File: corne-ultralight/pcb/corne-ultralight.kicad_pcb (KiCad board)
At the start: 2 copper layers, 275.5 x 105.6 mm, 130 parts, among them J2 OLED, J5 Breakaway_Tabs, J7 OLED, SW1 SW_PUSH, SW10 SW_PUSH, SW11 SW_PUSH, SW12 SW_PUSH, SW13 SW_PUSH, SW14 SW_PUSH, SW15 SW_PUSH, SW16 SW_PUSH, SW17 SW_PUSH, SW18 SW_PUSH, SW19 SW_PUSH, SW2 SW_PUSH, SW20 SW_PUSH, SW21 SW_PUSH, SW22 SW_PUSH, SW23 SW_PUSH, SW24 SW_PUSH, SW25 SW_PUSH, SW26 SW_PUSH, SW27 SW_PUSH, SW28 SW_PUSH, SW29 SW_PUSH, SW3 SW_PUSH, SW30 SW_PUSH, SW31 SW_PUSH, SW32 SW_PUSH, SW33 SW_PUSH, SW34 SW_PUSH, SW35 SW_PUSH, SW36 SW_PUSH, SW37 SW_PUSH, SW38 SW_PUSH, SW39 SW_PUSH, SW4 SW_PUSH, SW40 SW_PUSH, SW41 SW_PUSH, SW42 SW_PUSH, SW5 SW_PUSH, SW6 SW_PUSH, SW7 SW_PUSH, SW8 SW_PUSH, SW9 SW_PUSH, U1 xiao-ble, U2 ProMicro

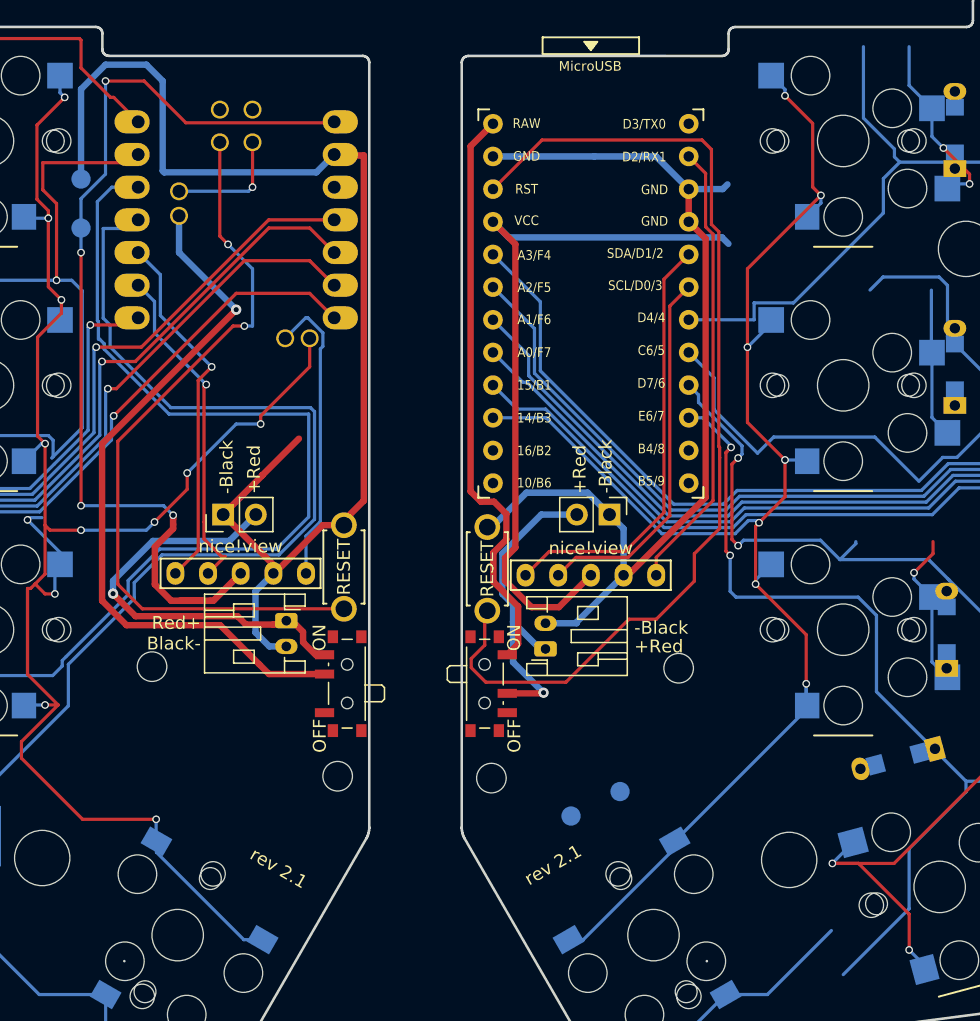
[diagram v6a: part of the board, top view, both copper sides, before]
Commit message: Moved nice!view VCC to 3.3v
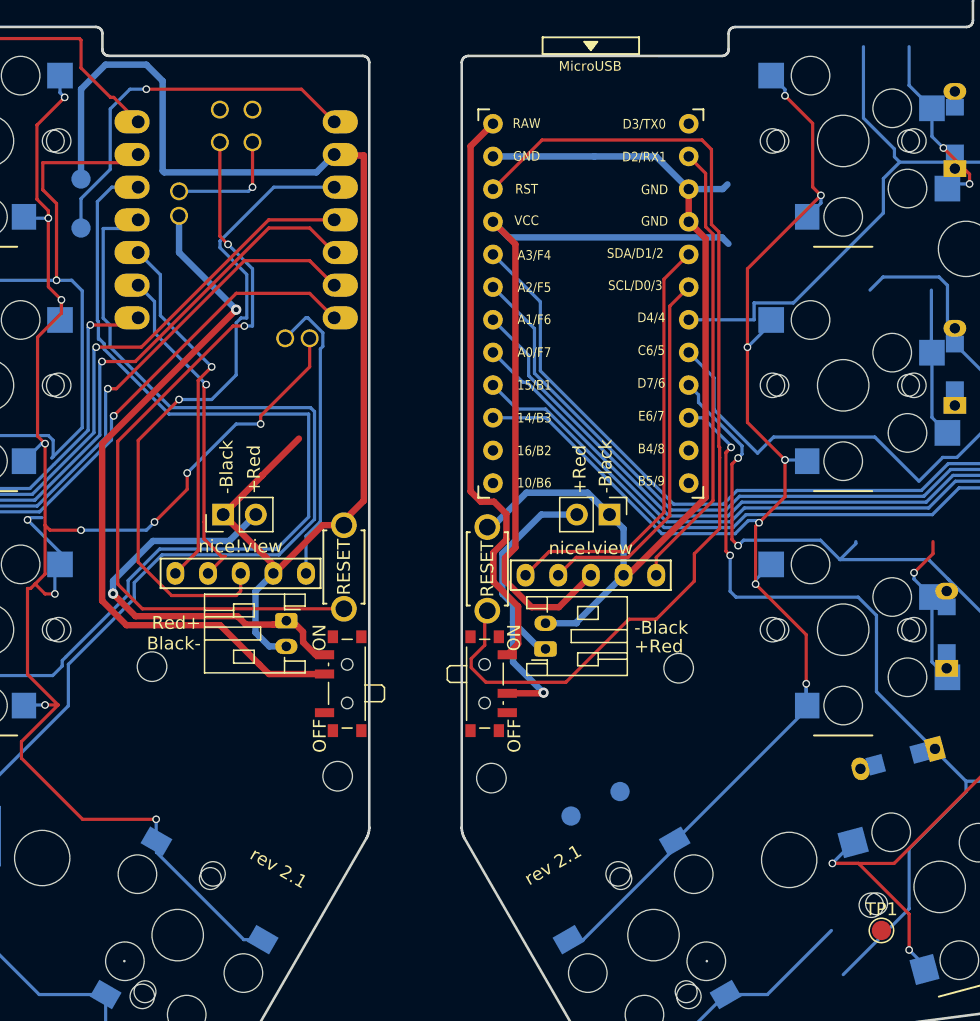
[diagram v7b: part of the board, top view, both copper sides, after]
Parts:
- added TP1: RGB, TestPoint:TestPoint_Pad_D1.5mm, F.Cu at (186.7, 104.9)
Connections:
- J2 pad 3: VCC -> VDDL
- U1 pad 12: unconnected-(U1-Pad12) -> VDDL
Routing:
- net VDDL: track 0.00 -> 52.2 mm, vias 0 -> 1
- net VCC: track 76.6 -> 29.6 mm, vias 4 -> 1
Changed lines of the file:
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@@
   (net 71 "col4_r")
   (net 72 "col5_r")
-  (net 73 "unconnected-(U1-Pad12)")
+  (net 73 "RGB")
   (net 74 "CS")
   (net 75 "unconnected-(U2-Pad14)")
@@
   (net 88 "+5V")
   (net 89 "unconnected-(U2-Pad1)")
+  (net 90 "VDDL")
   (footprint "kbd:ResetSW_1side" (layer "F.Cu")
     (at 156.0125 76.817432 -90)
@@
     (fp_arc (start 2.28 7.45) (mid 2.595908 6.48733) (end 3.5 6.03) (layer "B.SilkS") (width 0.15))
     (fp_arc (start 3.825 -6.804) (mid 5.347189 -6.33089) (end 6.089 -4.92) (layer "B.SilkS") (width 0.15))
-    (fp_arc (start 2.57 1.4) (mid 1.834422 2.975843) (end 0.2 3.57) (layer "B.SilkS") (width 0.15))
+    (fp_arc (start 2.57 1.4) (mid 1.834421 2.975843) (end 0.2 3.57) (layer "B.SilkS") (width 0.15))
     (fp_arc (start 0.225 -2.8) (mid 1.744361 -2.328061) (end 2.485 -0.92) (layer "B.SilkS") (width 0.15))
     (fp_line (start 2.275 8.225) (end -2.275 8.225) (layer "F.SilkS") (width 0.15))
@@
       (net 35 "SCL") (pinfunction "Pin_2") (pintype "passive"))
     (pad "3" thru_hole oval (at 5.08 0) (size 1.397 1.778) (drill 0.8128) (layers *.Cu "B.Mask")
-      (net 27 "VCC") (pinfunction "Pin_3") (pintype "passive"))
+      (net 90 "VDDL") (pinfunction "Pin_3") (pintype "passive"))
     (pad "4" thru_hole oval (at 7.62 0) (size 1.397 1.778) (drill 0.8128) (layers *.Cu "B.Mask")
       (net 26 "GND") (pinfunction "Pin_4") (pintype "passive"))
@@
     )
   )
+  (footprint "TestPoint:TestPoint_Pad_D1.5mm" (layer "F.Cu")
+    (at 186.6575 104.93)
+    (descr "SMD pad as test Point, diameter 1.5mm")
+    (tags "test point SMD pad")
+    (property "Sheetfile" "corne-ultralight.kicad_sch")
+    (property "Sheetname" "")
+    (attr exclude_from_pos_files)
+    (fp_text reference "TP1" (at 0 -1.648) (layer "F.SilkS")
+      (effects (font (size 1 1) (thickness 0.15)))
+    )
+    (fp_text value "RGB" (at 0 1.75) (layer "F.Fab")
+      (effects (font (size 1 1) (thickness 0.15)))
+    )
+    (fp_text user "${REFERENCE}" (at 0 -1.65) (layer "F.Fab")
+      (effects (font (size 1 1) (thickness 0.15)))
+    )
+    (fp_circle (center 0 0) (end 0 0.95) (layer "F.SilkS") (width 0.12) (fill none))
+    (fp_circle (center 0 0) (end 1.25 0) (layer "F.CrtYd") (width 0.05) (fill none))
+    (pad "1" smd circle (at 0 0) (size 1.5 1.5) (layers "F.Cu" "F.Mask")
+      (net 73 "RGB") (pinfunction "1") (pintype "passive"))
+  )
   (footprint "Connector_PinHeader_2.54mm:PinHeader_1x02_P2.54mm_Vertical" (layer "F.Cu")
     (at 165.5125 72.595 -90)
@@
       (net 29 "col1") (pinfunction "A6_MOSI/1.15") (pintype "bidirectional"))
     (pad "12" thru_hole oval (at 7.62 -2.54 180) (size 2.75 1.8) (drill 1 (offset -0.475 0)) (layers *.Cu *.Mask)
-      (net 73 "unconnected-(U1-Pad12)") (pinfunction "3V3") (pintype "power_out+no_connect"))
+      (net 90 "VDDL") (pinfunction "3V3") (pintype "power_out"))
     (pad "13" thru_hole oval (at 7.62 -5.08 180) (size 2.75 1.8) (drill 1 (offset -0.475 0)) (layers *.Cu *.Mask)
       (net 26 "GND") (pinfunction "GND") (pintype "power_out"))
@@
   (segment (start 138.275 82.0575) (end 137.9875 81.77) (width 0.5) (layer "B.Cu") (net 26))
   (segment (start 139.0625 82.845) (end 138.275 82.0575) (width 0.5) (layer "B.Cu") (net 26))
-  (segment (start 124.4225 52.22) (end 124.4225 71.905) (width 0.25) (layer "F.Cu") (net 27))
-  (segment (start 134.7115 79.295) (end 136.8385 77.168) (width 0.508) (layer "F.Cu") (net 27))
-  (segment (start 132.576412 42.1315) (end 144.036 42.1315) (width 0.25) (layer "F.Cu") (net 27))
-  (segment (start 131.5845 72.598) (end 131.5845 72.648) (width 0.508) (layer "F.Cu") (net 27))
-  (segment (start 126.3275 38.885) (end 129.329912 38.885) (width 0.25) (layer "F.Cu") (net 27))
-  (segment (start 144.036 42.1315) (end 144.1075 42.06) (width 0.25) (layer "F.Cu") (net 27))
-  (segment (start 130.1625 75.114) (end 131.5845 73.692) (width 0.508) (layer "F.Cu") (net 27))
-  (segment (start 133.8625 79.295) (end 131.4375 79.295) (width 0.508) (layer "F.Cu") (net 27))
-  (segment (start 131.5845 73.373) (end 131.5845 73.692) (width 0.508) (layer "F.Cu") (net 27))
-  (segment (start 130.1625 78.02) (end 130.1625 75.114) (width 0.508) (layer "F.Cu") (net 27))
-  (segment (start 131.4375 79.295) (end 130.1625 78.02) (width 0.508) (layer "F.Cu") (net 27))
-  (segment (start 129.329912 38.885) (end 132.576412 42.1315) (width 0.25) (layer "F.Cu") (net 27))
-  (segment (start 132.1255 79.295) (end 133.8625 79.295) (width 0.508) (layer "F.Cu") (net 27))
+  (segment (start 141.5675 39.52) (end 144.1075 42.06) (width 0.25) (layer "F.Cu") (net 27))
+  (segment (start 129.5025 39.52) (end 141.5675 39.52) (width 0.25) (layer "F.Cu") (net 27))
   (segment (start 144.432345 42.695) (end 144.1075 42.695) (width 0.508) (layer "F.Cu") (net 27))
-  (segment (start 133.8625 79.295) (end 134.4625 79.295) (width 0.508) (layer "F.Cu") (net 27))
-  (segment (start 131.5845 72.648) (end 131.5845 72.923) (width 0.508) (layer "F.Cu") (net 27))
-  (segment (start 134.4625 79.295) (end 134.7115 79.295) (width 0.508) (layer "F.Cu") (net 27))
-  (segment (start 131.5845 72.923) (end 131.5845 73.373) (width 0.508) (layer "F.Cu") (net 27))
-  (via (at 131.5845 72.648) (size 0.6) (drill 0.4) (layers "F.Cu" "B.Cu") (net 27))
-  (via (at 126.3275 38.885) (size 0.6) (drill 0.4) (layers "F.Cu" "B.Cu") (net 27))
-  (via (at 124.4225 71.905) (size 0.6) (drill 0.4) (layers "F.Cu" "B.Cu") (net 27))
-  (via (at 124.4225 52.22) (size 0.6) (drill 0.4) (layers "F.Cu" "B.Cu") (net 27))
-  (segment (start 124.4225 48.02528) (end 126.3275 46.12028) (width 0.25) (layer "B.Cu") (net 27))
-  (segment (start 124.4225 50.315) (end 124.4225 52.22) (width 0.25) (layer "B.Cu") (net 27))
-  (segment (start 130.8415 71.905) (end 131.5845 72.648) (width 0.25) (layer "B.Cu") (net 27))
-  (segment (start 124.4225 71.905) (end 130.8415 71.905) (width 0.25) (layer "B.Cu") (net 27))
-  (segment (start 126.3275 46.12028) (end 126.3275 38.885) (width 0.25) (layer "B.Cu") (net 27))
+  (via (at 129.5025 39.52) (size 0.6) (drill 0.4) (layers "F.Cu" "B.Cu") (net 27))
+  (segment (start 126.6925 45.75528) (end 126.6925 41.06) (width 0.25) (layer "B.Cu") (net 27))
+  (segment (start 128.2325 39.52) (end 129.5025 39.52) (width 0.25) (layer "B.Cu") (net 27))
   (segment (start 124.4225 50.315) (end 124.4225 48.02528) (width 0.25) (layer "B.Cu") (net 27))
+  (segment (start 124.4225 48.02528) (end 126.6925 45.75528) (width 0.25) (layer "B.Cu") (net 27))
+  (segment (start 126.6925 41.06) (end 128.2325 39.52) (width 0.25) (layer "B.Cu") (net 27))
   (segment (start 27.6485 71.904508) (end 27.140746 71.396754) (width 0.25) (layer "F.Cu") (net 28))
   (segment (start 26.042499 44.555001) (end 27.9025 42.695) (width 0.25) (layer "F.Cu") (net 28))
@@
   (segment (start 137.4395 47.458) (end 132.0425 47.458) (width 0.25) (layer "B.Cu") (net 88))
   (segment (start 137.7575 47.14) (end 137.4395 47.458) (width 0.25) (layer "B.Cu") (net 88))
+  (segment (start 128.8675 66.825) (end 128.8675 76.294) (width 0.25) (layer "F.Cu") (net 90))
+  (segment (start 136.8385 78.539) (end 136.8385 77.168) (width 0.25) (layer "F.Cu") (net 90))
+  (segment (start 136.4875 78.89) (end 136.8385 78.539) (width 0.25) (layer "F.Cu") (net 90))
+  (segment (start 132.0425 63.65) (end 128.8675 66.825) (width 0.25) (layer "F.Cu") (net 90))
+  (segment (start 128.8675 76.294) (end 131.4635 78.89) (width 0.25) (layer "F.Cu") (net 90))
+  (segment (start 131.4635 78.89) (end 136.4875 78.89) (width 0.25) (layer "F.Cu") (net 90))
+  (via (at 132.0425 63.65) (size 0.6) (drill 0.4) (layers "F.Cu" "B.Cu") (net 90))
+  (segment (start 139.413616 47.14) (end 135.2275 51.326116) (width 0.25) (layer "B.Cu") (net 90))
+  (segment (start 144.1075 47.14) (end 139.413616 47.14) (width 0.25) (layer "B.Cu") (net 90))
+  (segment (start 136.863616 57.31) (end 136.4875 57.686116) (width 0.25) (layer "B.Cu") (net 90))
+  (segment (start 135.2275 51.843884) (end 137.3075 53.923884) (width 0.25) (layer "B.Cu") (net 90))
+  (segment (start 137.3075 57.31) (end 136.863616 57.31) (width 0.25) (layer "B.Cu") (net 90))
+  (segment (start 136.4875 61.745) (end 134.5825 63.65) (width 0.25) (layer "B.Cu") (net 90))
+  (segment (start 136.4875 57.686116) (end 136.4875 61.745) (width 0.25) (layer "B.Cu") (net 90))
+  (segment (start 134.5825 63.65) (end 132.0425 63.65) (width 0.25) (layer "B.Cu") (net 90))
+  (segment (start 137.3075 53.923884) (end 137.3075 57.31) (width 0.25) (layer "B.Cu") (net 90))
+  (segment (start 135.2275 51.326116) (end 135.2275 51.843884) (width 0.25) (layer "B.Cu") (net 90))
 )

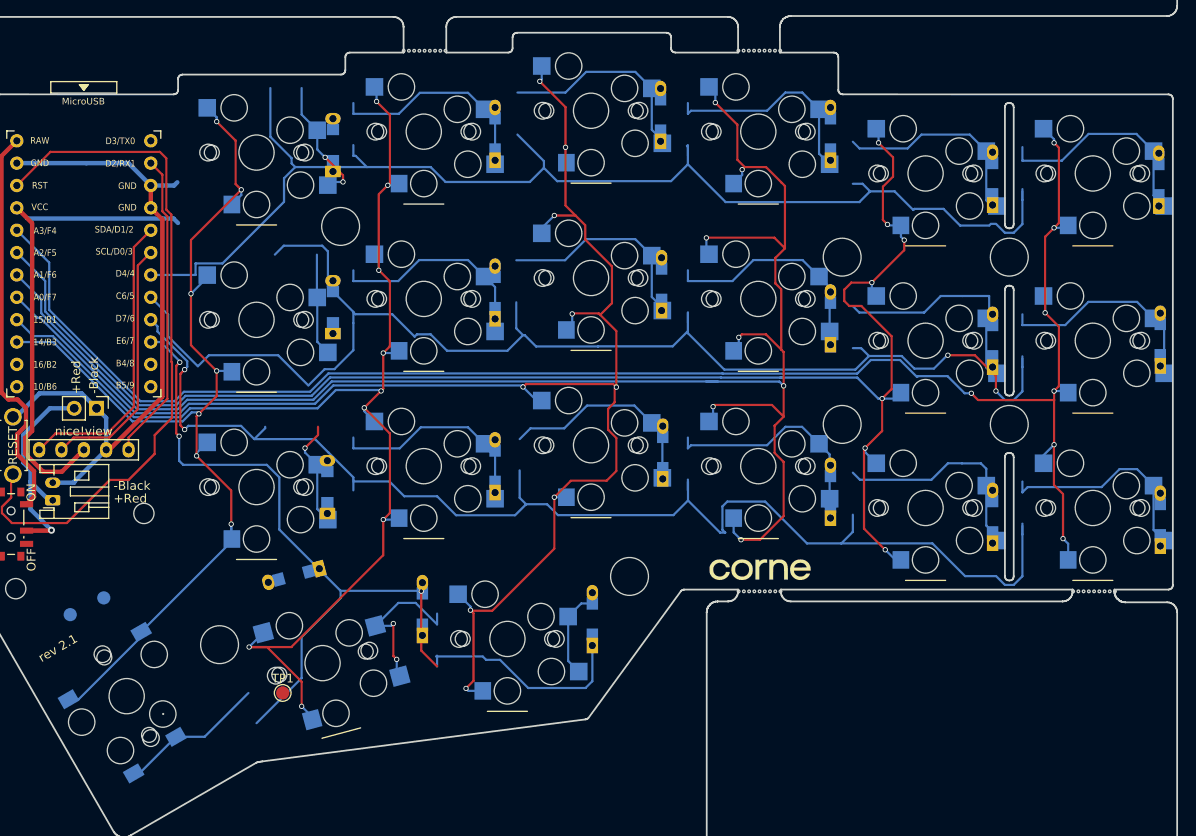
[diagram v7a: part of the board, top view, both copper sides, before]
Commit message: rebased with proper right footprints
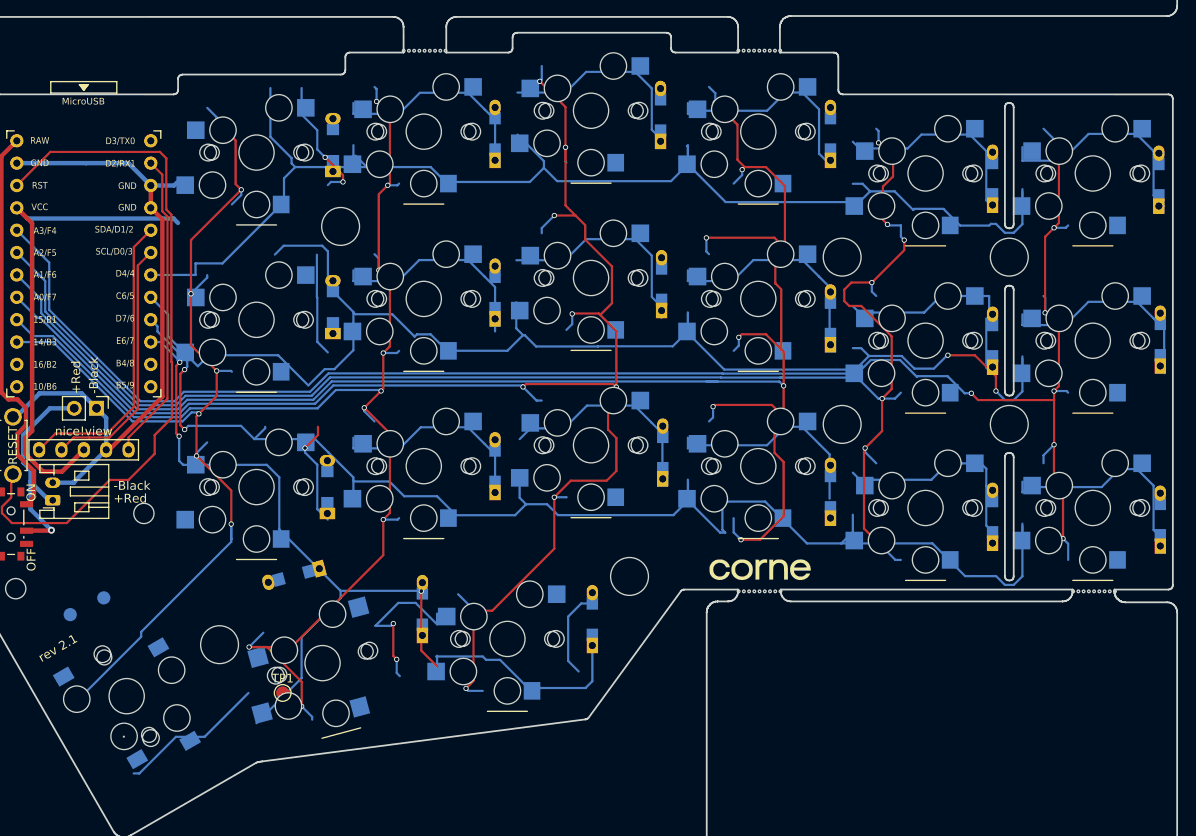
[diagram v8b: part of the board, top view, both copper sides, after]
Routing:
- net row3_r: track 106.0 -> 933.6 mm, vias 3 -> 29
- net col0_r: track 192.8 -> 0.00 mm, vias 7 -> 0
- net col1_r: track 179.3 -> 0.00 mm, vias 7 -> 0
- net row2_r: track 146.9 -> 0.00 mm, vias 2 -> 0
- net row1_r: track 152.3 -> 24.4 mm, vias 2 -> 0
- net col5_r: track 118.7 -> 0.00 mm, vias 7 -> 0
- net row0_r: track 143.3 -> 182.4 mm, vias 0 -> 2
- net Net-(D29-Pad2): track 25.3 -> 0.00 mm
- net Net-(D24-Pad2): track 24.7 -> 0.00 mm
- net Net-(D31-Pad2): track 24.4 -> 0.00 mm
- net col3_r: track 183.9 -> 207.6 mm
- net Net-(D25-Pad2): track 23.7 -> 0.00 mm
- net Net-(D40-Pad2): track 10.1 -> 28.8 mm, vias 0 -> 2
- net Net-(D41-Pad2): track 18.7 -> 0.00 mm, vias 2 -> 0
- net Net-(D27-Pad2): track 14.5 -> 0.00 mm, vias 2 -> 0
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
